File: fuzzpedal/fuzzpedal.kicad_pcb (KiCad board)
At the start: 2 copper layers, 60 x 112.1 mm, 71 parts, among them J1 PWR JACK, J2 Wire connector (smol), J3 Wire connector (circuit), Q1 BC239, Q2 BC239, Q3 BC239, Q4 BC239

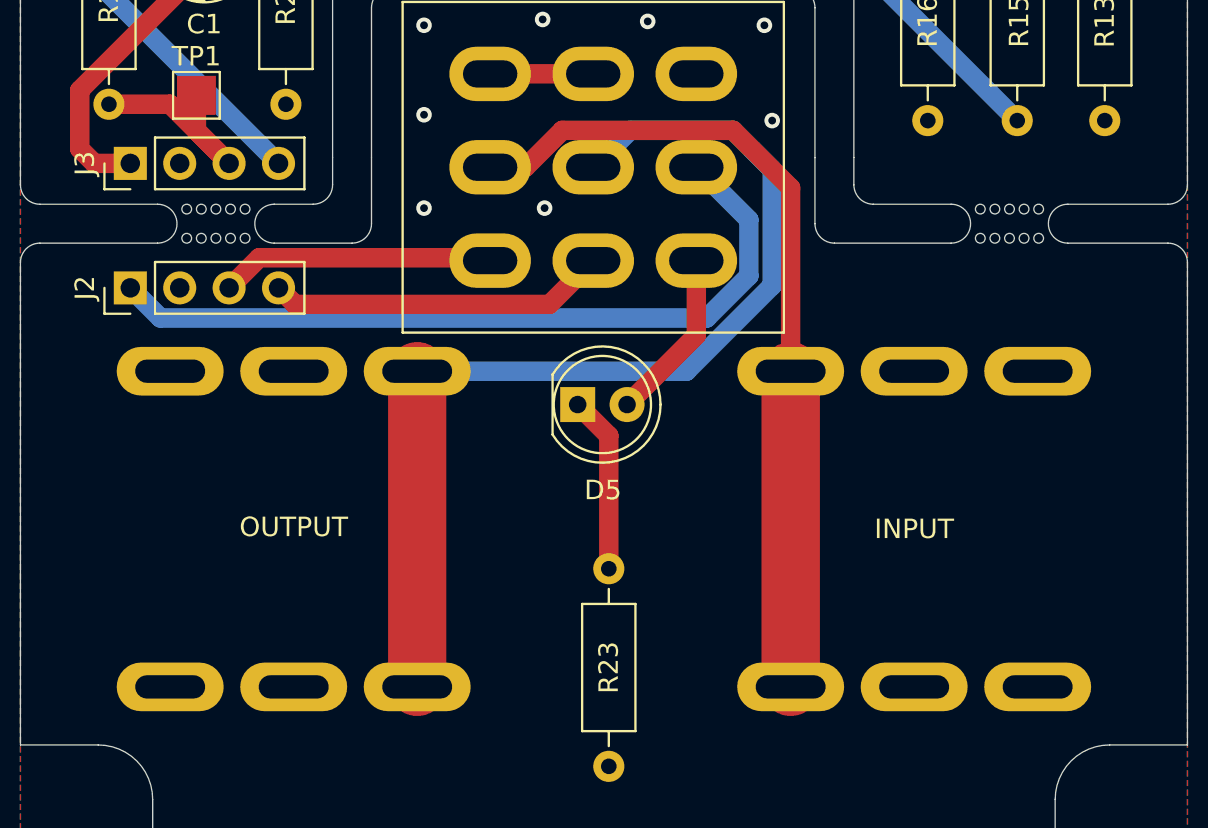
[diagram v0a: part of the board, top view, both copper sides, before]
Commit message: fix: hole sizes of the jacks + bigger OSHW logo
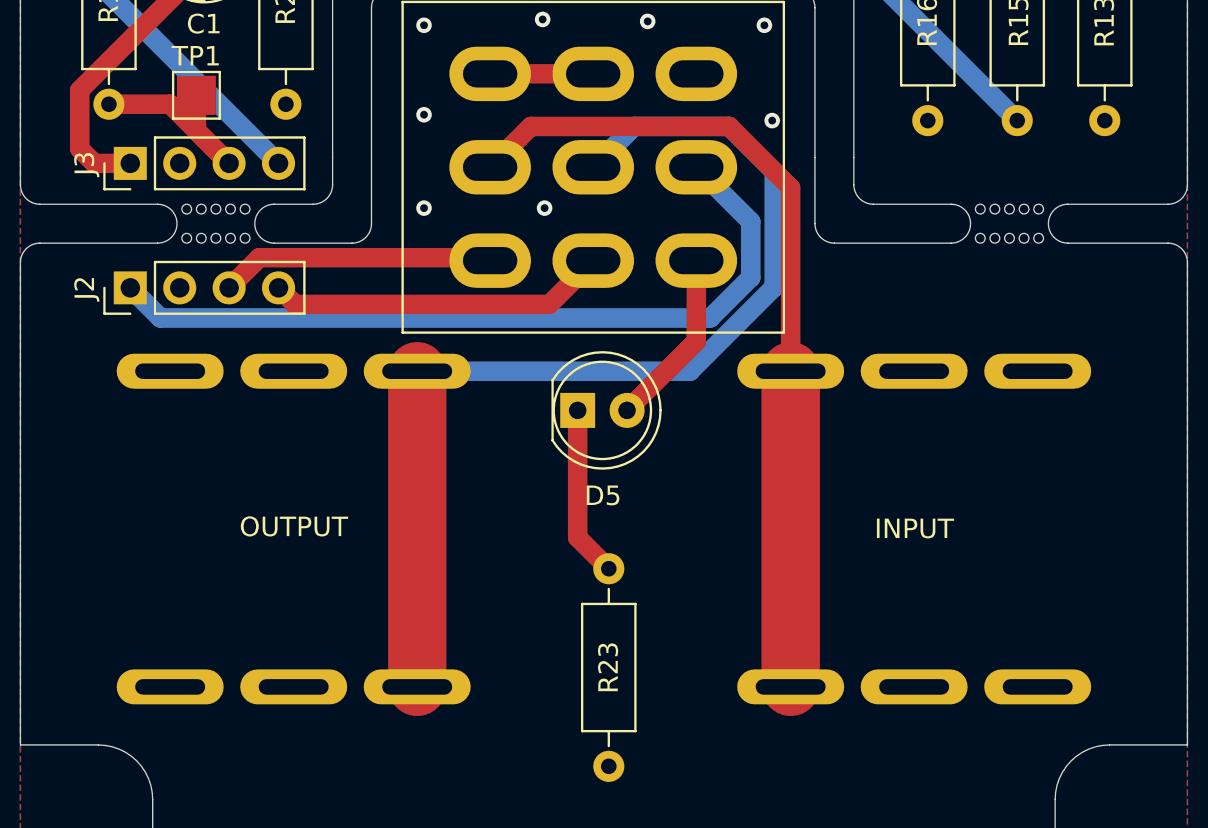
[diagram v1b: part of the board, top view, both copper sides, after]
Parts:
- removed the REF** at (162.7, 142.1)
- added REF**: OSHW-Logo2_14.6x12mm_SilkScreen, Symbol:OSHW-Logo2_14.6x12mm_SilkScreen, B.Cu at (162.7, 142.4)
- moved D5 0.30 mm to (145.8, 136.4)
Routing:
- net Net-(J4-PadT): track 54.5 -> 53.5 mm

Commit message: add: hw revision version to 2.1
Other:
- board text added: "alberand rev 2.1 2021"
- board text removed: "alberand rev 2.0 2020"
